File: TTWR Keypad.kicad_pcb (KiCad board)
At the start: 2 copper layers, 35.5 x 60 mm, 46 parts, among them J1 Conn_01x15, J2 Conn_01x15, U1 PTS526 SK15 SMTR2 LFS, U10 PTS526 SK15 SMTR2 LFS, U11 PTS526 SK15 SMTR2 LFS, U12 PTS526 SK15 SMTR2 LFS, U13 PTS526 SK15 SMTR2 LFS, U14 PTS526 SK15 SMTR2 LFS, U15 PTS526 SK15 SMTR2 LFS, U16 PTS526 SK15 SMTR2 LFS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

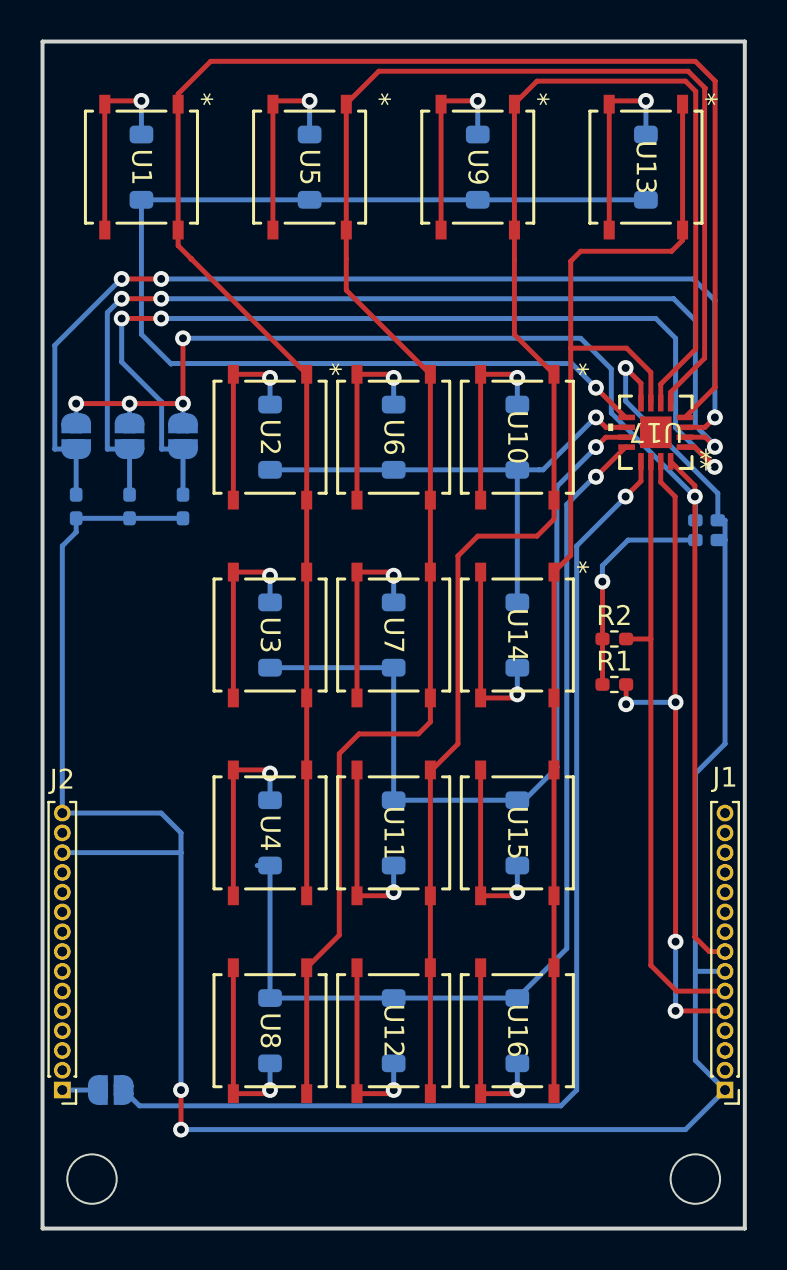
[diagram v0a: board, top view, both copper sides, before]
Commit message: Rev 1. New layout on 4 layer board. Changed package/footprint of the IO Expander to SOP-16.
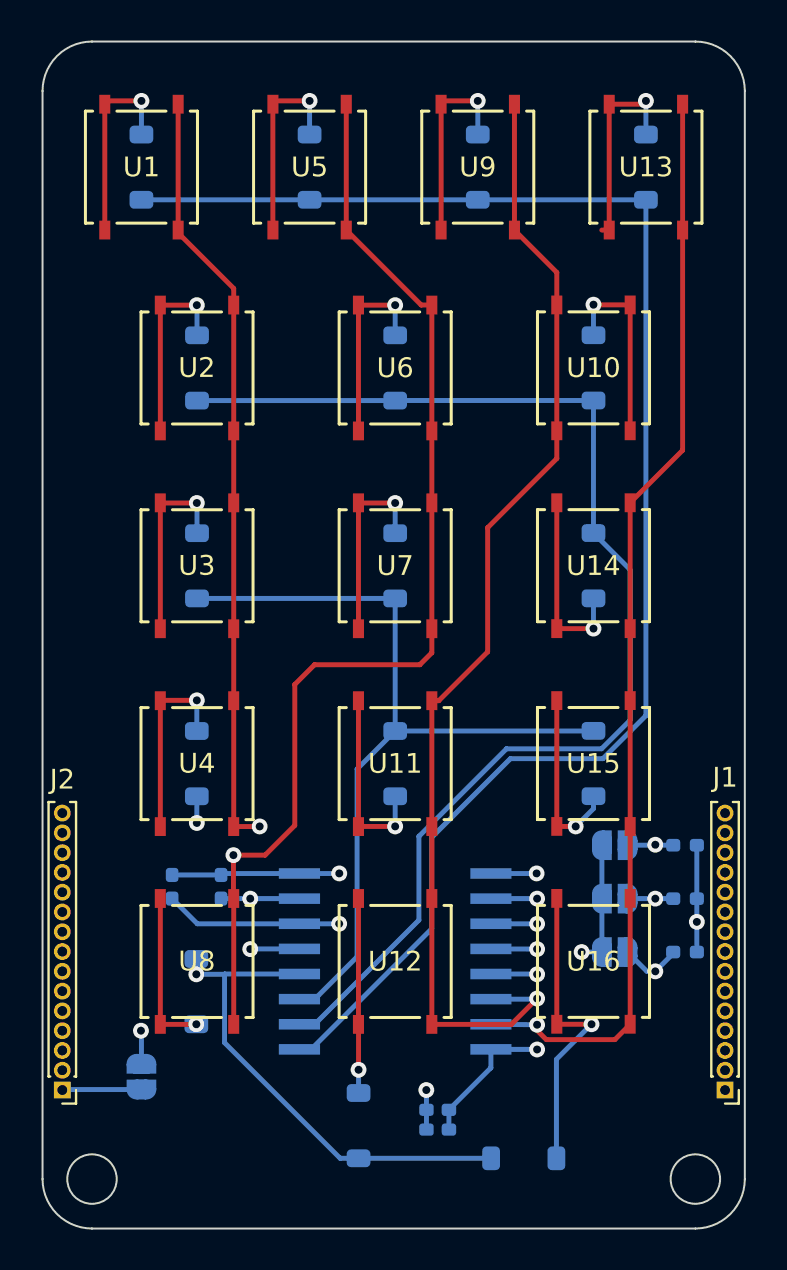
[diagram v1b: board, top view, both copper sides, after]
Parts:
- R1, R2: moved to B.Cu
- U17: footprint footprints:PCF8574RGTR -> footprints:SOT162-1_NXP-M; moved to B.Cu
- moved R5 38.1 mm to (182.5, 86.0), turned to 0 degrees
- moved JP3 37.7 mm to (178.9, 86.0), turned to 0 degrees
- moved R4 34.4 mm to (182.5, 83.3), turned to 0 degrees
- moved JP2 33.9 mm to (178.9, 83.3), turned to 0 degrees
- moved C1 32.8 mm to (170.0, 94.0)
- moved C2 32.8 mm to (170.0, 95.0)
- moved R3 30.6 mm to (182.5, 80.6), turned to 0 degrees
- moved JP1 30.1 mm to (178.9, 80.6), turned to 0 degrees
- moved U17 29.8 mm to (167.8, 86.5)
- moved R2 25.6 mm to (156.6, 82.7), turned to -90 degrees
- moved R1 22.4 mm to (159.0, 82.7), turned to -90 degrees
- moved D16 6.46 mm to (174.3, 96.5), turned to 0 degrees
- moved D10 5.21 mm to (177.8, 56.5)
- moved D14 5.21 mm to (177.8, 66.5)
- moved D15 5.21 mm to (177.8, 76.5)
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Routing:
- net GND: track 120.3 -> 32.6 mm, vias 3 -> 2
- net /IO Expander/INT: track 56.7 -> 13.3 mm, vias 1 -> 2
- net /IO Expander/A2: track 51.5 -> 12.5 mm, vias 3 -> 2
- net /IO Expander/A1: track 49.7 -> 10.7 mm, vias 3 -> 2
- net /IO Expander/A0: track 48.6 -> 11.3 mm, vias 3 -> 2
- net ROW_1: track 26.0 -> 62.5 mm, vias 1 -> 0
- net COL_0: track 89.1 -> 57.9 mm, vias 0 -> 2
- net +3.3V: track 82.3 -> 52.2 mm, vias 6 -> 3
- net COL_2: track 81.6 -> 58.5 mm, vias 0 -> 1
- net ROW_0: track 58.6 -> 78.8 mm, vias 1 -> 0
- net ROW_3: track 50.1 -> 34.4 mm, vias 1 -> 2
- net COL_1: track 92.0 -> 77.3 mm, vias 0 -> 2
- net COL_3: track 61.5 -> 55.5 mm, vias 0 -> 1
- net Net-(D16-A): track 9.64 -> 15.6 mm
- net /IO Expander/SCL: track 31.0 -> 34.7 mm, vias 0 -> 1
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- added copper zone on In2.Cu, net GND
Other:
- outline, holes or cut-outs redrawn
- copper layers 2 -> 4
